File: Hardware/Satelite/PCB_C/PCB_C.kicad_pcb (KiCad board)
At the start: 2 copper layers, 54 x 54 mm, 52 parts, among them IC1 MCP1501T-33E_CHY, IC2 IS25LP080D-JULE-TR, IC3 BQ24392RSER, IC4 MS563702BA03-50, IC5 BMX055, J1 Conn_01x06, J2 JUMPER, J3 Conector_PCB_B-C, J4 Conector_Expansion_CanSat, J5 USB_B_Micro, Q1 BC817, U1 NTB0104BQ,115, U2 TCA9802DGKR, U3 STM32F303RETx, U4 NTB0104BQ,115, U5 SN74LVC1G3157DCKR, U6 Si7006-A20-IM1, Y1 LFXTAL016178, Y2 Crystal

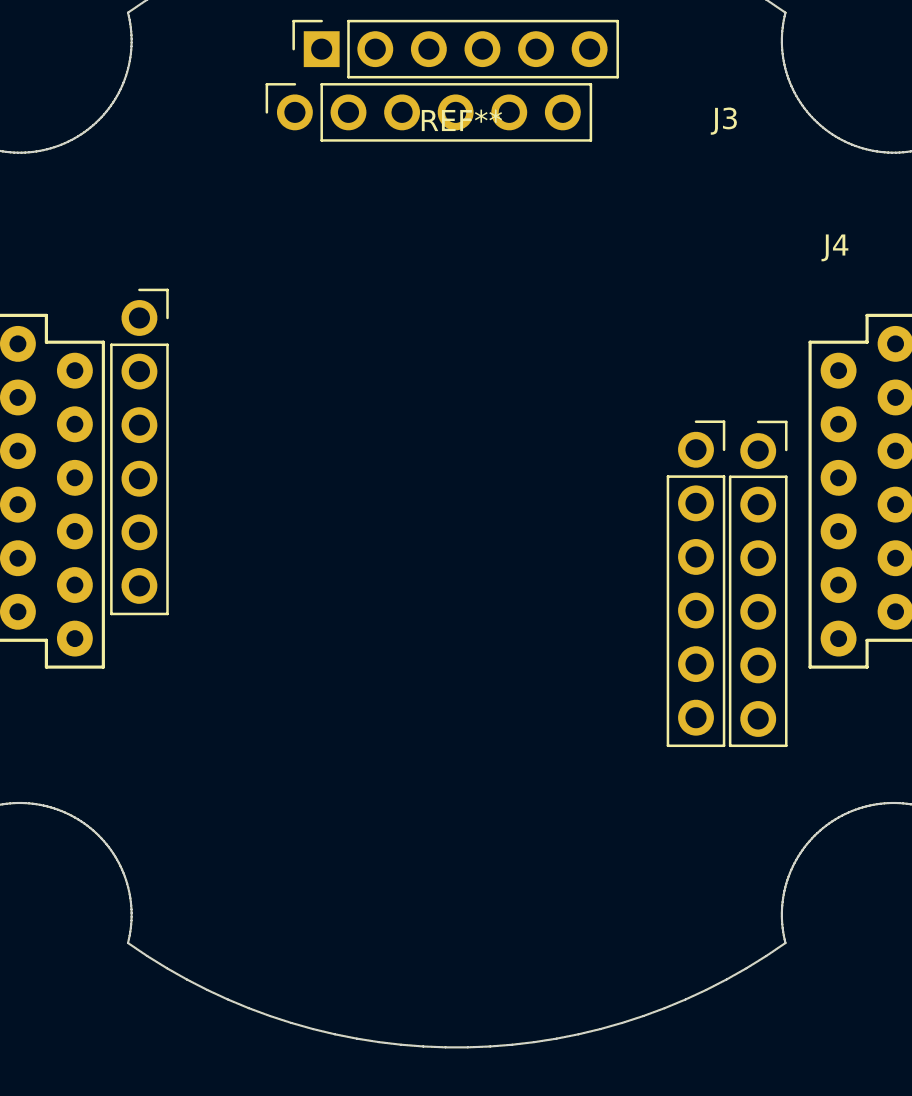
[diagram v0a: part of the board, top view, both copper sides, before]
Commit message: Agregados agujeros de montaje para PCB C
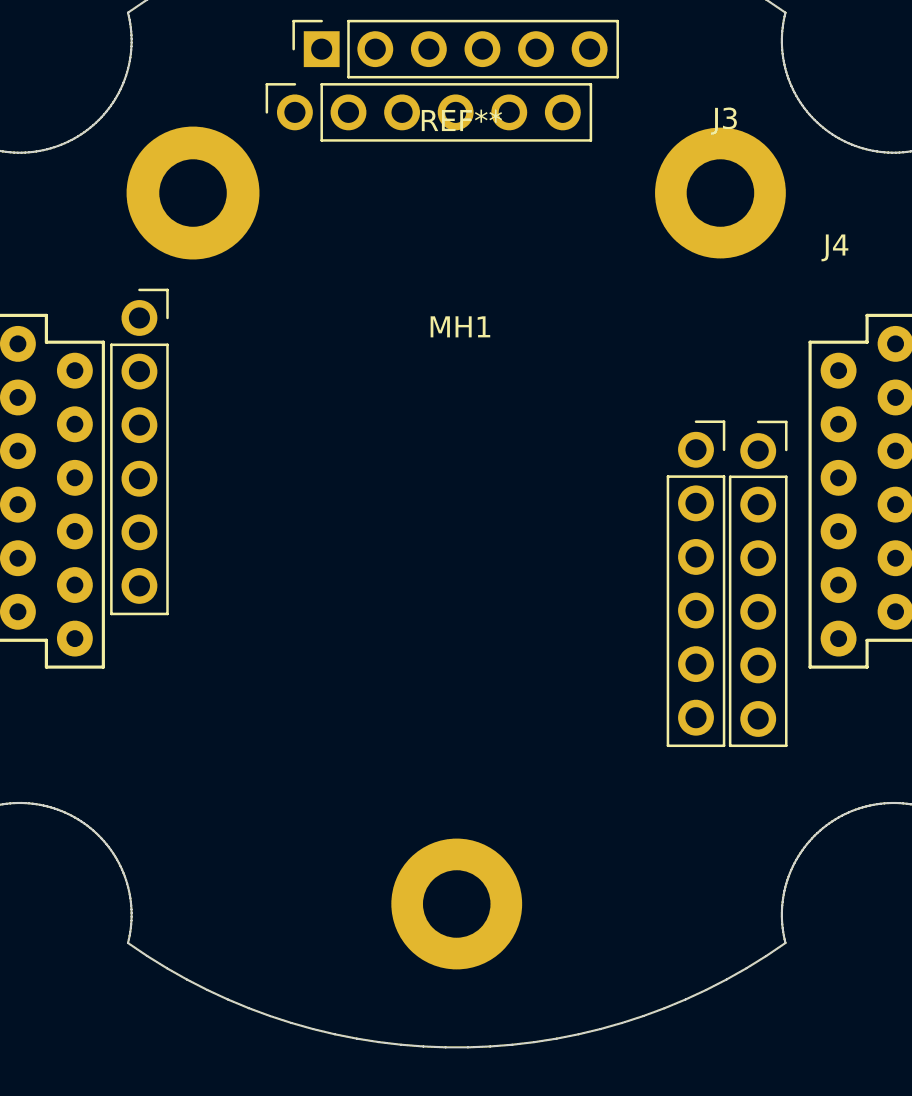
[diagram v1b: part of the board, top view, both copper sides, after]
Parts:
- added MH1: MH_CanSat, AXTEC:MH_CanSat, F.Cu at (0.00, 0.00)
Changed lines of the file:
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@@
     (tracks 0)
     (zones 0)
-    (modules 52)
+    (modules 53)
     (nets 108)
   )
@@
       (effects (font (size 1 1) (thickness 0.15)))
     )
-    (fp_text value Conector_PCB_B-C (at 0 -23.5) (layer F.Fab)
+    (fp_text value Conector_PCB_B-C (at 0 -30) (layer F.Fab)
       (effects (font (size 1 1) (thickness 0.15)))
     )
@@
       (effects (font (size 1 1) (thickness 0.15)))
     )
-    (fp_text value Conector_Expansion_CanSat (at 0 -24.13) (layer F.Fab)
+    (fp_text value Conector_Expansion_CanSat (at 15 -10) (layer F.Fab)
       (effects (font (size 1 1) (thickness 0.15)))
     )
@@
     (fp_line (start 19.925604 -15.47029) (end 20.1004 -15.44702) (layer Edge.Cuts) (width 0.1))
   )
+  (module AXTEC:MH_CanSat (layer F.Cu)
+    (at 0 0)
+    (fp_text reference MH1 (at 0.17 -7.12) (layer F.SilkS)
+      (effects (font (size 1 1) (thickness 0.15)))
+    )
+    (fp_text value MH_CanSat (at 0.03 -8.47) (layer F.Fab)
+      (effects (font (size 1 1) (thickness 0.15)))
+    )
+    (pad 2 thru_hole circle (at 12.5 -13.5) (size 6.2 6.2) (drill 3.2) (layers *.Cu *.Mask)
+      (net 1 GND))
+    (pad 1 thru_hole circle (at -12.5 -13.5) (size 6.3 6.3) (drill 3.2) (layers *.Cu *.Mask)
+      (net 1 GND))
+    (pad 3 thru_hole circle (at 0 20.2) (size 6.2 6.2) (drill 3.2) (layers *.Cu *.Mask)
+      (net 1 GND))
+  )
 )

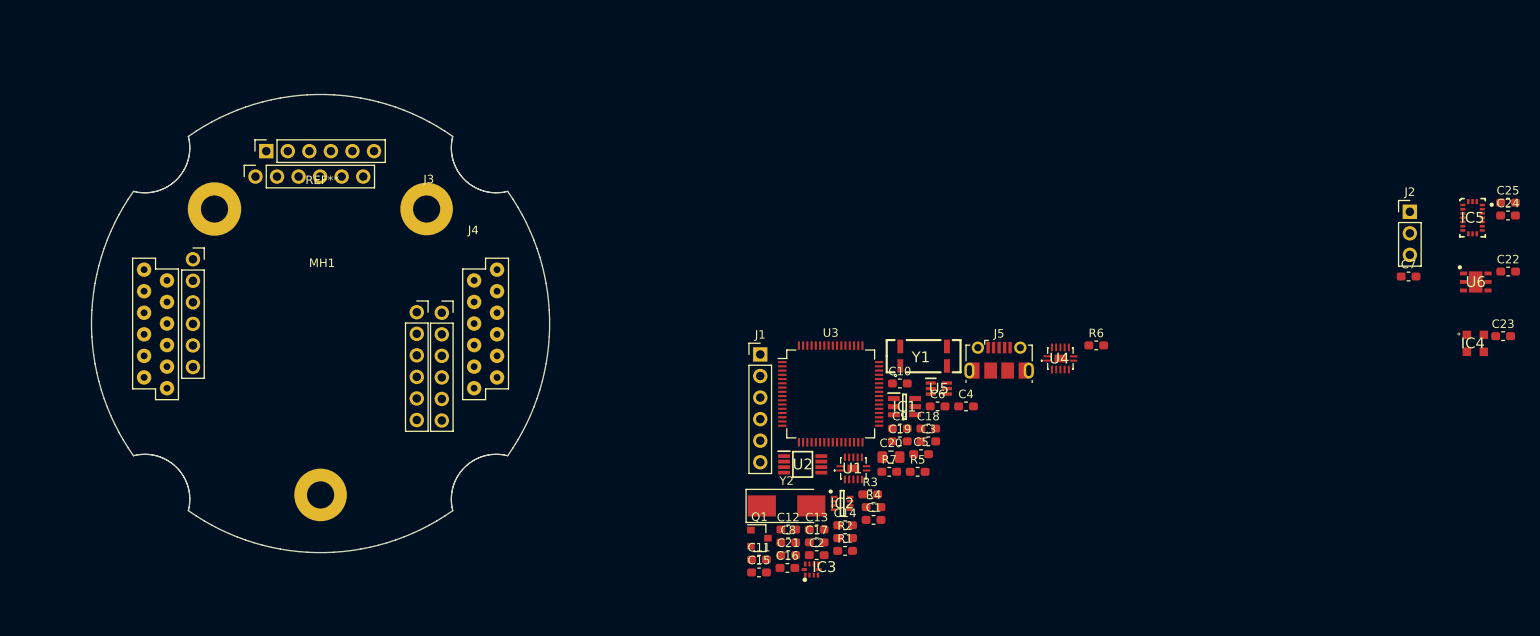
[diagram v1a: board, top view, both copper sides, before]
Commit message: Capacitores 0402 para PCB_C
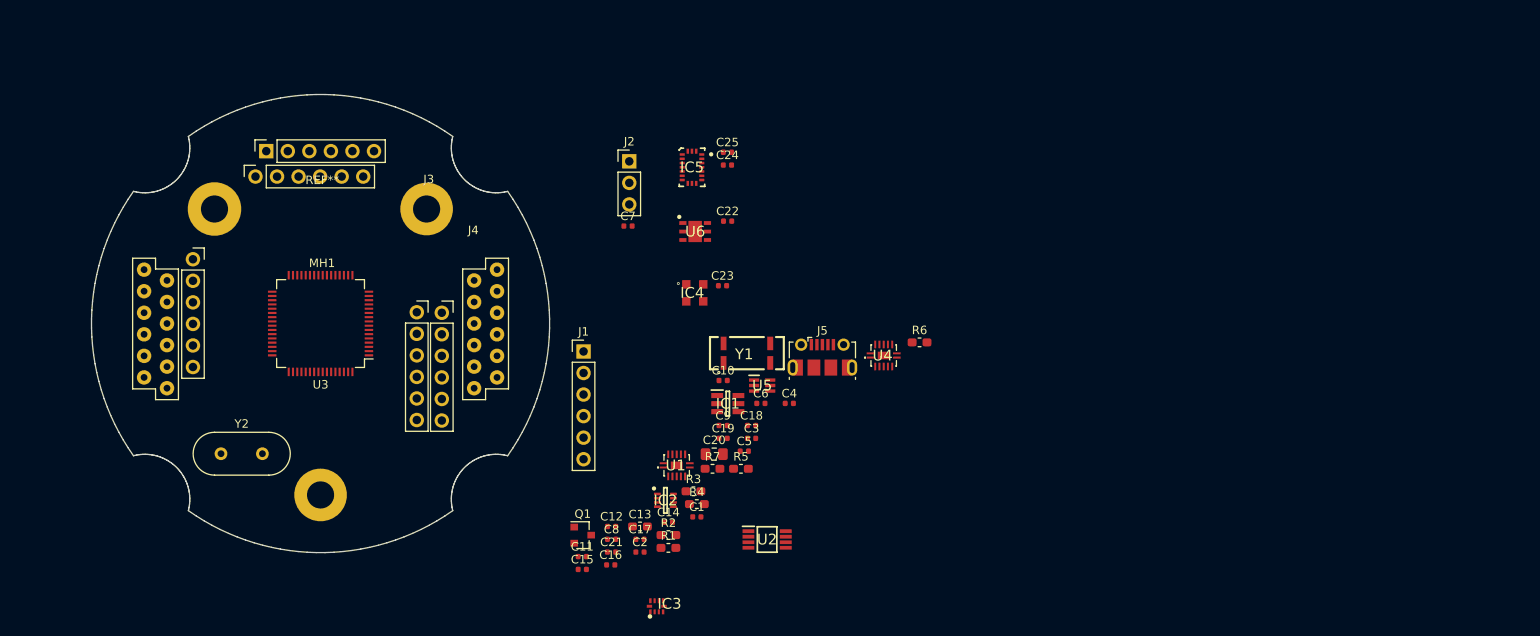
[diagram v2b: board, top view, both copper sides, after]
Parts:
- C1, C10, C11, C12, C14, C15, C16, C17, C18, C19, C2, C21, C22, C23, C24, C25, C3, C4, C5, C6, C7, C8, C9: footprint Capacitor_SMD:C_0603_1608Metric_Pad1.05x0.95mm_HandSolder -> Capacitor_SMD:C_0402_1005Metric
- Y2: footprint Crystal:Crystal_SMD_0603-2Pin_6.0x3.5mm_HandSoldering -> Crystal:Crystal_HC49-4H_Vertical
- moved C24 92.2 mm to (48.0, -18.7)
- moved C25 92.2 mm to (48.0, -20.2)
- moved C7 92.2 mm to (36.2, -11.5)
- moved IC5 92.2 mm to (43.8, -18.4)
- moved U6 92.2 mm to (44.2, -10.8)
- moved C22 92.2 mm to (48.0, -12.1)
- moved C23 92.2 mm to (47.4, -4.46)
- moved IC4 92.2 mm to (44.1, -3.61)
- moved J2 92.2 mm to (36.4, -19.1)
- moved Y2 66.9 mm to (-11.7, 15.3)
- moved U3 60.7 mm to (0.00, 0.00), turned to 180 degrees
- moved C10 20.8 mm to (47.4, 6.71)
- moved C11 20.8 mm to (30.8, 27.5)
- moved C14 20.8 mm to (41.0, 23.4)
- moved C15 20.8 mm to (30.8, 29.0)
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
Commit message: Diseño inicial de PCB C (WIP)
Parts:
- C10, C12, C14, C18, Y2: moved to B.Cu
- C13: footprint Capacitor_SMD:C_0603_1608Metric_Pad1.05x0.95mm_HandSolder -> Capacitor_SMD:C_0402_1005Metric
- moved R6 96.9 mm to (-24.0, 23.1)
- moved U5 79.4 mm to (-26.4, 19.8)
- moved R5 72.5 mm to (-23.0, 16.9)
- moved J5 70.2 mm to (-8.59, 22.3), turned to 338 degrees
- moved R7 66.7 mm to (-20.2, 23.1), turned to 180 degrees
- moved C18 58.6 mm to (-7.20, 3.60), turned to 90 degrees
- moved C14 55.0 mm to (-6.70, -4.00)
- moved Q1 53.3 mm to (-22.1, 20.1), turned to 90 degrees
- moved C20 51.5 mm to (0.50, -7.90), turned to 180 degrees
- moved IC3 49.8 mm to (-7.57, 17.6), turned to 180 degrees
- moved C3 48.6 mm to (2.29, 11.0), turned to 270 degrees
- moved C10 47.3 mm to (0.20, 3.80), turned to 180 degrees
- moved C4 46.9 mm to (8.38, 11.0), turned to 270 degrees
- moved J1 46.4 mm to (-6.50, -24.1), turned to 90 degrees
- moved Y1 45.9 mm to (5.38, 13.3), turned to 270 degrees
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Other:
- net class Default: trace_width 0.25 -> 0.2; via_dia 0.8 -> 0.6; via_drill 0.4 -> 0.3

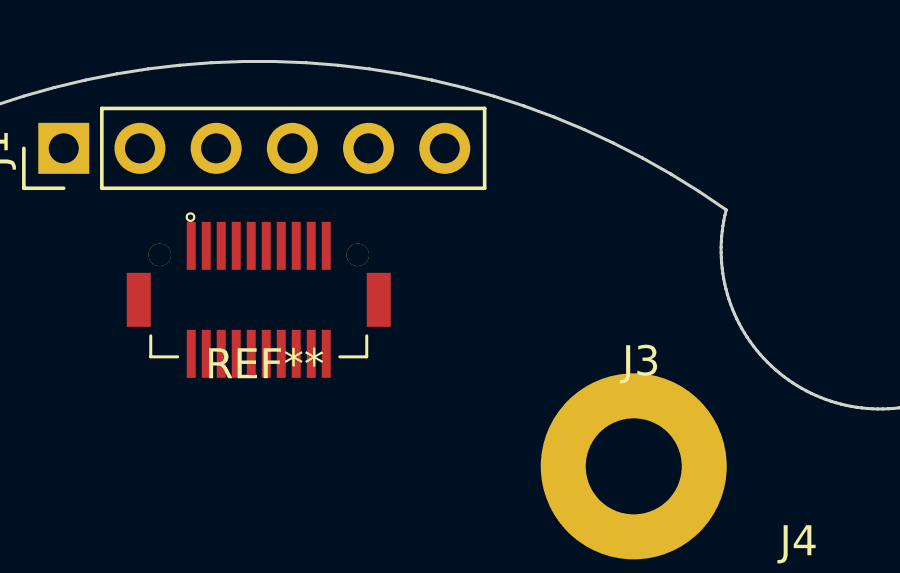
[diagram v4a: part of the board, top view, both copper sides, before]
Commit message: La parte del conector B-C que va en el PCB_B fue movido a bottom mientras que la parte que va en el PCB_C permanece en top
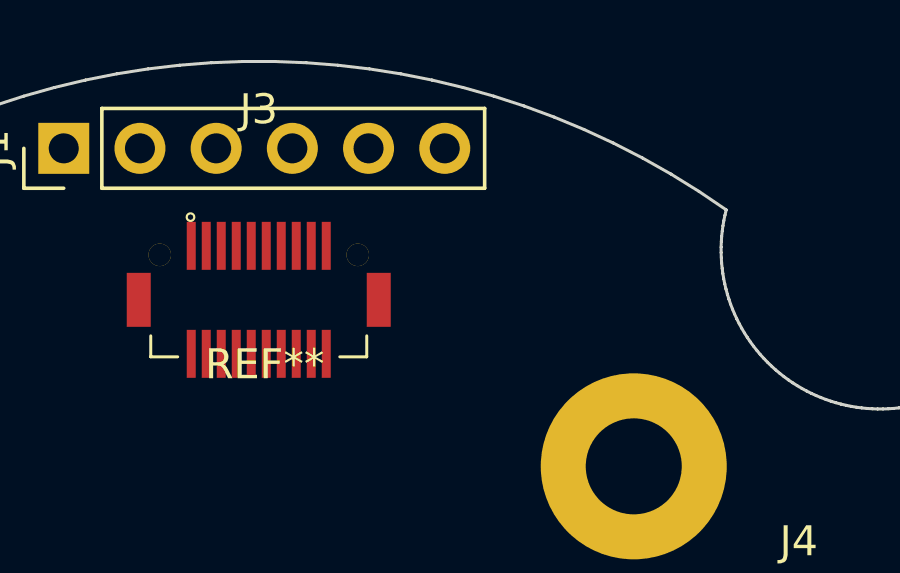
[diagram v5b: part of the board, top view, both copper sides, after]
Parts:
- J3: value Conector_PCB_B-C -> Conector_PCB_B-C_Lado_C; footprint AXTEC:Conector_PCB_B-C -> AXTEC:Conector_PCB_B-C_Lado_C
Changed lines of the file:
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@@
     (add_net VDD)
   )
-  (module AXTEC:Conector_PCB_B-C (layer F.Cu)
+  (module AXTEC:Conector_PCB_B-C_Lado_C (layer F.Cu)
     (at 0 0)
-    (fp_text reference J3 (at 12.75 -17) (layer F.SilkS)
+    (fp_text reference J3 (at 0 -25.4) (layer F.SilkS)
       (effects (font (size 1 1) (thickness 0.15)))
     )
-    (fp_text value Conector_PCB_B-C (at 0 -30) (layer F.Fab)
+    (fp_text value Conector_PCB_B-C_Lado_C (at 0 -23.5) (layer F.Fab)
       (effects (font (size 1 1) (thickness 0.15)))
     )

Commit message: PCB C (WIP)
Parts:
- C15, C16, C17, C6: moved to B.Cu
- J3: value Conector_PCB_B-C_Lado_C -> Conector_PCB_B-C
- moved C11 96.7 mm to (-27.1, -27.2)
- moved C9 96.7 mm to (-30.5, -27.2)
- moved U2 96.7 mm to (-28.8, -24.5)
- moved J2 94.3 mm to (-34.0, -9.65)
- moved C6 66.2 mm to (-0.30, 0.81), turned to 180 degrees
- moved C19 54.6 mm to (22.9, -32.1)
- moved C2 54.6 mm to (29.4, -23.8)
- moved C21 54.6 mm to (22.9, -34.4)
- moved C5 54.6 mm to (29.4, -26.3)
- moved U1 54.6 mm to (32.8, -25.0)
- moved U4 54.6 mm to (26.3, -33.3)
- moved C15 41.4 mm to (-1.27, -2.54), turned to 270 degrees
- moved C17 38.7 mm to (-4.32, -2.54), turned to 270 degrees
- moved C16 37.5 mm to (-2.79, -2.54), turned to 270 degrees
- moved C13 30.2 mm to (-33.5, 10.1)
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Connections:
- J3 pad 10: GND -> /I_SENSE_3V3
- J3 pad 11: /V_SENSE_5V -> /V_SENSE_3V3
- J3 pad 12: /V_SENSE_3V3 -> /V_SENSE_5V
- J3 pad 13: /P1 -> GND
- J3 pad 14: /GPS_TX -> +5V
- J3 pad 15: /GPOUT -> GND
- J3 pad 16: /CHG -> GND
- J3 pad 17: +3V3_Internal -> GND
- J3 pad 18: /CHG_DISABLE -> +3V3
- J3 pad 19: /SCLK -> +BATT
- J3 pad 2: +3V3 -> +BATT
- J3 pad 20: /CS -> +BATT
- J3 pad 21: /SDI -> /I_SENSE_BATT
- J3 pad 22: /SDO -> /GPS_TX
- J3 pad 23: /S_PARACAIDAS -> /P1
- J3 pad 24: /S_GLOBO -> /SCLK
- J3 pad 25: +5V -> /CS
- J3 pad 26: /ISET -> /SDI
- J3 pad 27: VBUS -> /SDO
- J3 pad 28: /SDA -> /S_PARACAIDAS
- J3 pad 29: /SCL -> /S_GLOBO
- J3 pad 3: GND -> +3V3
- J3 pad 30: /I_SENSE_BATT -> /GPOUT
- J3 pad 31: (no net) -> /SDA
- J3 pad 32: (no net) -> /SCL
- J3 pad 33: (no net) -> /CHG_DISABLE
- J3 pad 34: (no net) -> /ISET
- J3 pad 35: (no net) -> /CHG
- J3 pad 36: (no net) -> GND
- J3 pad 37: (no net) -> GND
- J3 pad 38: (no net) -> GND
- J3 pad 39: (no net) -> GND
- J3 pad 40: (no net) -> GND
- J3 pad 41: (no net) -> Net-(J3-Pad41)
- J3 pad 42: (no net) -> Net-(J3-Pad42)
- J3 pad 43: (no net) -> Net-(J3-Pad43)
- J3 pad 44: (no net) -> Net-(J3-Pad44)
- J3 pad 5: /I_SENSE_5V -> GND
- J3 pad 6: /I_SENSE_3V3 -> GND
- J3 pad 7: +BATT -> +5V
- J3 pad 8: +3V3 -> GND
- J3 pad 9: GND -> /I_SENSE_5V
- U3 pad 23: /I_SENSE_BATT -> /I_SENSE_5V
- U3 pad 26: /I_SENSE_5V -> /I_SENSE_BATT
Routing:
- net GND: track 0.00 -> 70.5 mm, vias 0 -> 19
- net +BATT: track 0.00 -> 52.3 mm
- net +5V: track 0.00 -> 37.4 mm
- net +3V3: track 0.00 -> 34.9 mm
- net +3V3_Internal: track 0.00 -> 17.5 mm, vias 0 -> 4
- net Net-(C4-Pad1): track 0.00 -> 17.0 mm
- net Net-(C3-Pad1): track 0.00 -> 14.0 mm
- net /FLASH_CS: track 0.00 -> 11.0 mm
- net Net-(C7-Pad1): track 0.00 -> 7.36 mm
- net /V_SENSE_3V3: track 0.00 -> 7.15 mm, vias 0 -> 1
- net Net-(C8-Pad1): track 0.00 -> 6.98 mm
- net /+VREF: track 0.00 -> 6.09 mm
- net /I_SENSE_BATT: track 0.00 -> 5.73 mm, vias 0 -> 1
- net /I_SENSE_5V: track 0.00 -> 4.56 mm, vias 0 -> 1
- net /NRST: track 0.00 -> 2.36 mm, vias 0 -> 1
- added copper zone on F.Cu, net +BATT
- added copper zone on F.Cu, net GND

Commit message: Terminado PCB_C. Revisación y optimizaciones pendientes.
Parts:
- removed C15, C16, C17: 100nF, Capacitor_SMD:C_0402_1005Metric
- C22, R1, R2, R3, R4: moved to B.Cu
- moved C22 73.2 mm to (-22.8, 11.0), turned to 90 degrees
- moved C24 71.7 mm to (-16.9, 14.1), turned to 90 degrees
- moved U6 68.2 mm to (-20.0, 12.4), turned to 180 degrees
- moved IC5 66.6 mm to (-14.3, 14.1), turned to 180 degrees
- moved C23 65.9 mm to (-21.5, -13.8)
- moved IC4 65.6 mm to (-21.1, -11.2)
- moved C25 61.8 mm to (-11.9, 13.1)
- moved C21 58.1 mm to (-10.3, 13.3), turned to 270 degrees
- moved U4 55.9 mm to (-10.2, 8.94), turned to 90 degrees
- moved R4 55.5 mm to (-11.4, 9.45), turned to 90 degrees
- moved R3 54.6 mm to (-9.50, 8.79), turned to 90 degrees
- moved C19 54.2 mm to (-8.43, 12.2), turned to 0 degrees
- moved J2 49.8 mm to (15.7, -8.94), turned to 135 degrees
- moved R1 48.9 mm to (-1.88, 7.37)
- moved C13 48.8 mm to (11.7, -8.48), turned to 0 degrees
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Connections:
- IC4 pad 2: /Sensor presión/SDA -> /SDA
- IC4 pad 3: /Sensor presión/SCL -> /SCL
- IC5 pad 11: /IMU/SDA -> /SDA
- IC5 pad 9: /IMU/SCL -> /SCL
- J3 pad 17: GND -> +3V3_Internal
- J3 pad 31: /SDA -> /SDA_CHG
- J3 pad 32: /SCL -> /SCL_CHG
- J3 pad 36: GND -> /3V_ENABLE
- J3 pad 37: GND -> /5V_ENABLE
- J4 pad 1: /EXT_IO0 -> Net-(J4-Pad1)
- J4 pad 2: /EXT_IO1 -> Net-(J4-Pad2)
- J4 pad 3: /EXT_IO2 -> /EXT_IO0
- J4 pad 4: /EXT_IO3 -> /EXT_IO1
- J4 pad 5: Net-(J4-Pad5) -> /EXT_IO2
- J4 pad 6: Net-(J4-Pad6) -> /EXT_IO3
- U3 pad 14: /I_SENSE_3V3 -> /I_SENSE_5V
- U3 pad 15: /V_SENSE_3V3 -> /I_SENSE_3V3
- U3 pad 17: /V_SENSE_5V -> /I_SENSE_BATT
- U3 pad 21: /I_SENSE_5V -> /V_SENSE_5V
- U3 pad 22: Net-(U3-Pad22) -> /SWITCH_IO_V
- U3 pad 23: /I_SENSE_5V -> Net-(U3-Pad23)
- U3 pad 26: /I_SENSE_BATT -> Net-(U3-Pad26)
- U3 pad 30: /I_SENSE_BATT -> Net-(U3-Pad30)
- U3 pad 39: /IO_A_EN -> /IO_EN
- U3 pad 50: /SWITCH_IO_V -> Net-(U3-Pad50)
- U3 pad 56: /5V_ENABLE -> /3V_ENABLE
- U3 pad 57: /3V_ENABLE -> /5V_ENABLE
- U3 pad 58: /ISET -> /GPOUT
- U3 pad 59: /GPOUT -> /CHG_DISABLE
- U3 pad 61: /CHG_DISABLE -> /ISET
- U6 pad 1: /Sensor temperatura y humedad/SDA -> /SDA
- U6 pad 6: /Sensor temperatura y humedad/SCL -> /SCL
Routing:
- net GND: track 70.5 -> 357.1 mm, vias 19 -> 32
- net +3V3_Internal: track 17.5 -> 188.1 mm, vias 4 -> 12
- net +3V3: track 34.9 -> 128.2 mm, vias 0 -> 6
- net VDD: track 0.00 -> 87.3 mm, vias 0 -> 10
- net /SCL: track 0.00 -> 62.2 mm, vias 0 -> 9
- net /SDA: track 0.00 -> 62.2 mm, vias 0 -> 9
- net /NRST: track 2.36 -> 58.7 mm, vias 1 -> 3
- net /SWDIO: track 0.00 -> 41.7 mm, vias 0 -> 2
- net /CHG: track 0.00 -> 36.8 mm
- net /CS: track 0.00 -> 35.9 mm, vias 0 -> 3
- net /I_SENSE_BATT: track 5.73 -> 41.6 mm, vias 1 -> 2
- net /ISET: track 0.00 -> 35.3 mm
- net /GPOUT: track 0.04 -> 35.1 mm, vias 0 -> 2
- net /5V_ENABLE: track 0.00 -> 34.7 mm, vias 0 -> 2
- net /SWO: track 0.00 -> 33.7 mm, vias 0 -> 2
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- added copper zone on B.Cu, net GND
